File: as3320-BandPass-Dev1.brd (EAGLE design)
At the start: 70.8 x 128.6 mm, 90 parts, among them IC1 CEM3320, IC2 TL074D, IC3 LM4040 5.0V, IC4 TL074D, IC5 TL072D

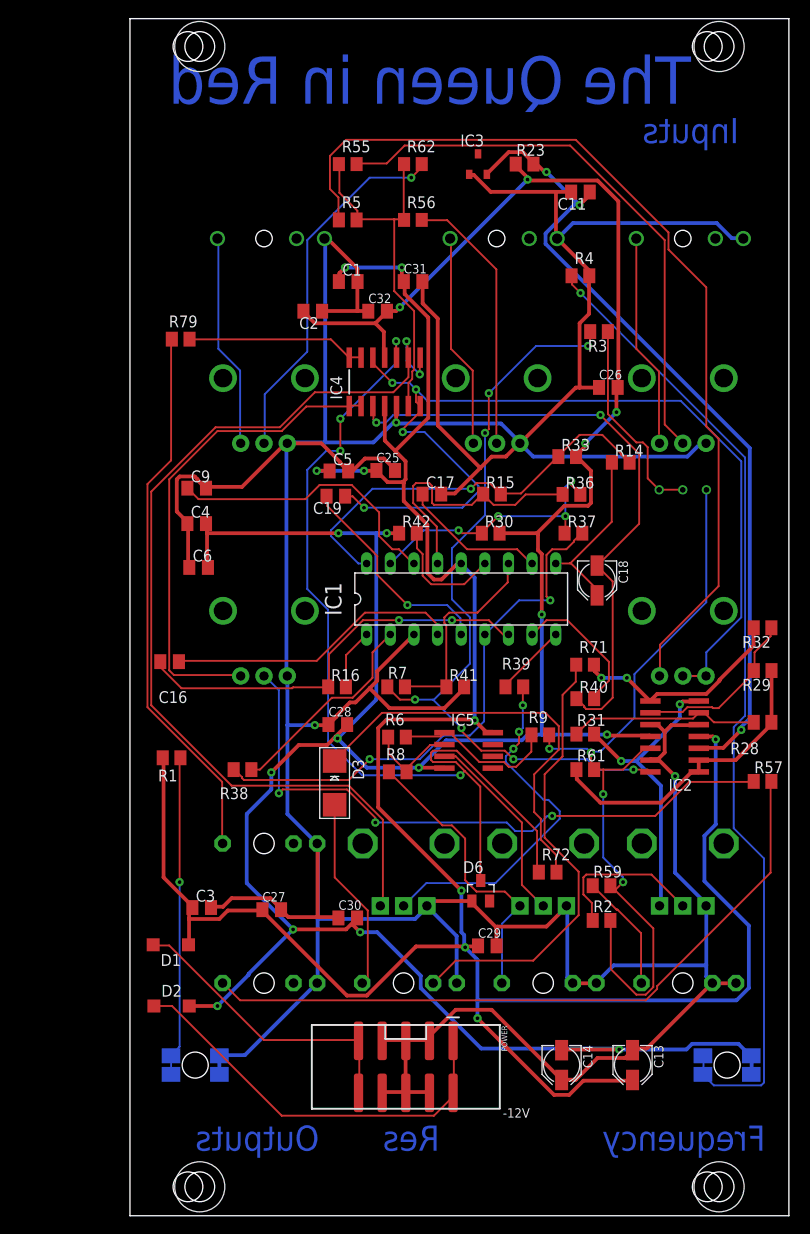
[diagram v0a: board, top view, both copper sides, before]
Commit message: Added 2nd output
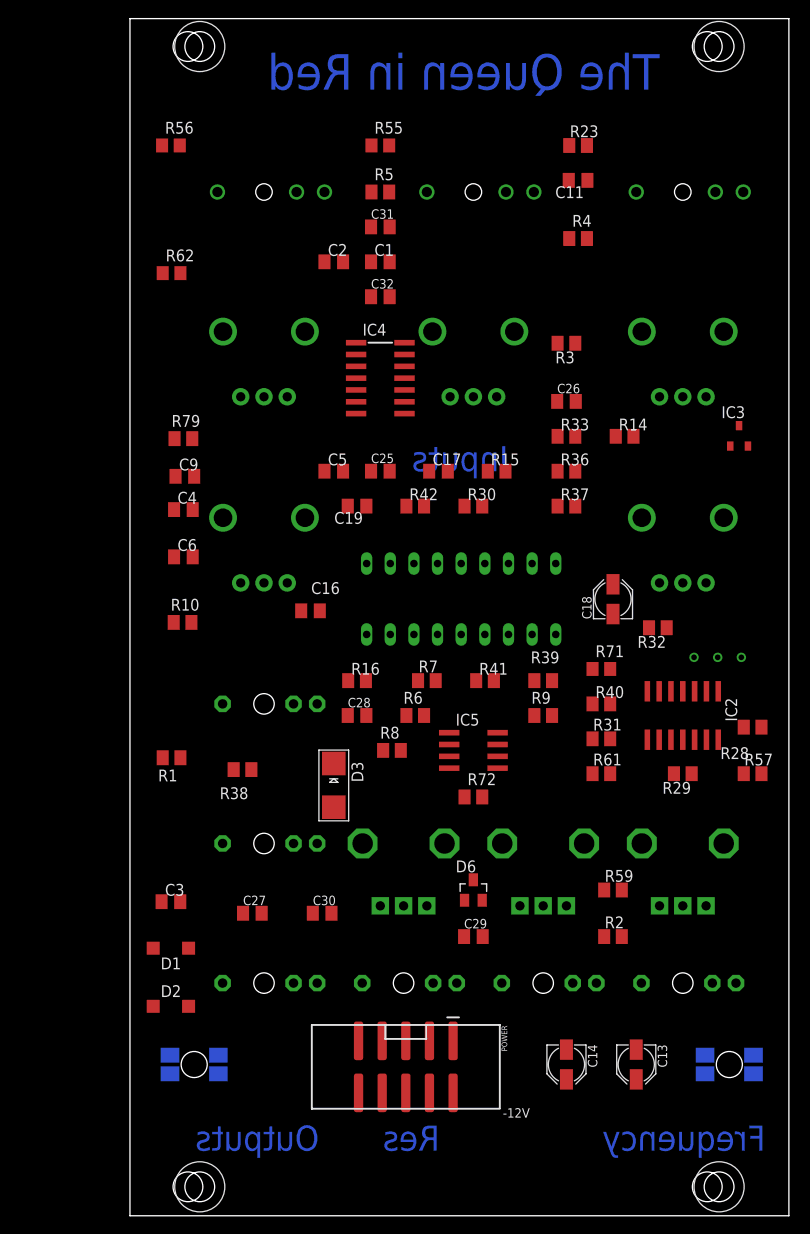
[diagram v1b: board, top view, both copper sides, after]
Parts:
- added INPUT_MIX: PJ301_THONKICONN6, og-pj301_variations:WQP_PJ_301M6
- added R10: 100K, Pure VCF:GMSN_M0805
- moved IC3 40.5 mm to (-13.9, 63.8)
- moved R62 28.5 mm to (-74.9, 81.3)
- moved R56 27.2 mm to (-75.0, 95.0)
- moved R60 18.4 mm to (-16.2, 40.0)
- moved C16 16.1 mm to (-60.0, 45.0)
- moved R29 14.0 mm to (-20.0, 27.5)
- moved R72 11.4 mm to (-42.5, 25.0)
- moved R32 11.2 mm to (-22.7, 43.2)
- moved R79 10.7 mm to (-73.7, 63.5)
- moved IN_GAIN 10.0 mm to (-20.0, 55.0)
- moved OUTPUTLEVEL 10.0 mm to (-65.0, 55.0)
- moved C31 6.84 mm to (-52.5, 86.2)
- moved R23 6.09 mm to (-31.2, 95.0)
- moved C2 5.77 mm to (-57.5, 82.5), turned to 0 degrees
- moved IN2 5.59 mm to (-42.5, 90.0)
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- renumbered IN_MIX to OUTPUT2, RES-2 to RES, V-OCT1 to V-OCT
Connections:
- removed net N$4: OUTPUTLEVEL.P$2, R57.1
- new net N$10: IC5.6, IC5.7
- new net N$11: IC5.5, OUTPUTLEVEL.P$2, R57.1
- new net N$14: R10.1
- new net O1: OUTPUT2.P3, R10.2
- net GND: now also INPUT_MIX.P1
- net N$1: no longer IC5.1
- net N$103: now also INPUT_MIX.P3; no longer OUTPUT2.P3
- net N$2: no longer IC5.2
- net N$7: no longer IC5.3
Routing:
- net GND: track 514.6 -> 0.00 mm, vias 3 -> 0
- net -12V: track 316.5 -> 0.00 mm, vias 15 -> 0
- net 12V: track 273.5 -> 0.00 mm, vias 9 -> 0
- net N$74: track 105.5 -> 0.00 mm, vias 1 -> 0
- net RESONANCE_IN2: track 105.0 -> 0.00 mm, vias 2 -> 0
- net BANDPASS_IN: track 103.9 -> 0.00 mm, vias 4 -> 0
- net N$89: track 103.9 -> 0.00 mm, vias 4 -> 0
- net N$20: track 101.0 -> 0.00 mm
- net -5VIN: track 88.6 -> 0.00 mm, vias 3 -> 0
- net N$12: track 88.0 -> 0.00 mm, vias 4 -> 0
- net N$3: track 83.7 -> 0.00 mm, vias 7 -> 0
- net O2: track 75.4 -> 0.00 mm
- net N$4: track 68.9 -> 0.00 mm, vias 3 -> 0
- net BANDPASS_OUT2: track 65.9 -> 0.00 mm, vias 2 -> 0
- net N$79: track 60.8 -> 0.00 mm
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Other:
- board text added: "Based on work by Forestcaver"

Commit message: Routed
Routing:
- net GND: track 0.00 -> 526.6 mm, vias 0 -> 3
- net -12V: track 0.00 -> 365.3 mm, vias 0 -> 11
- net 12V: track 0.00 -> 233.8 mm, vias 0 -> 13
- net N$36: track 0.00 -> 123.4 mm, vias 0 -> 3
- net N$30: track 0.00 -> 123.1 mm, vias 0 -> 2
- net N$74: track 0.00 -> 108.5 mm, vias 0 -> 1
- net N$3: track 0.00 -> 98.8 mm, vias 0 -> 8
- net N$89: track 0.00 -> 96.7 mm, vias 0 -> 4
- net N$11: track 0.00 -> 86.9 mm, vias 0 -> 3
- net O2: track 0.00 -> 82.2 mm
- net N$12: track 0.00 -> 81.2 mm, vias 0 -> 4
- net -5VIN: track 0.00 -> 80.1 mm
- net N$31: track 0.00 -> 80.0 mm
- net N$20: track 0.00 -> 74.1 mm, vias 0 -> 1
- net RESONANCE_IN2: track 0.00 -> 73.3 mm, vias 0 -> 1
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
